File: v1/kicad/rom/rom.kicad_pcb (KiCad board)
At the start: 2 copper layers, 68.5 x 69 mm, 2 parts, among them IC1 AT28C64B-15PU, U1 LNCPU Type A Connector

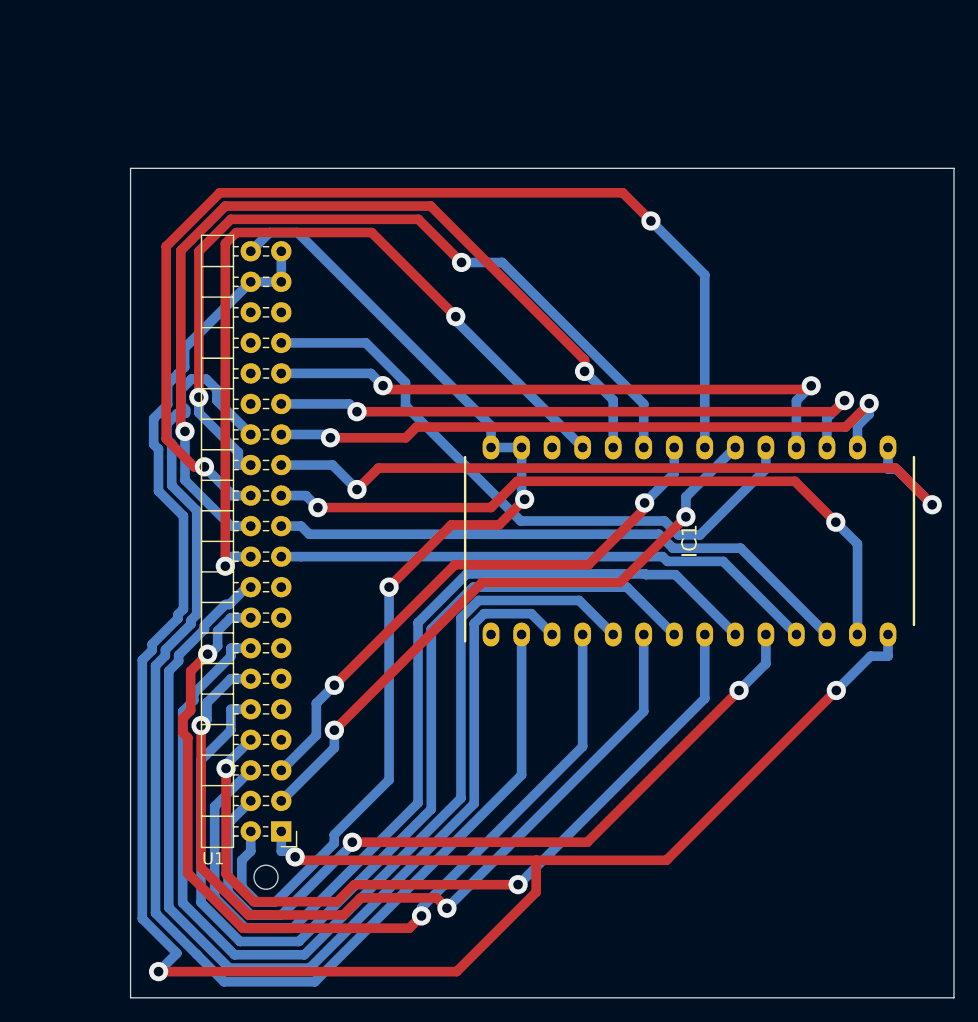
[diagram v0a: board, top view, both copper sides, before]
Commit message: readapt designs for BR, SP, SR, ALU
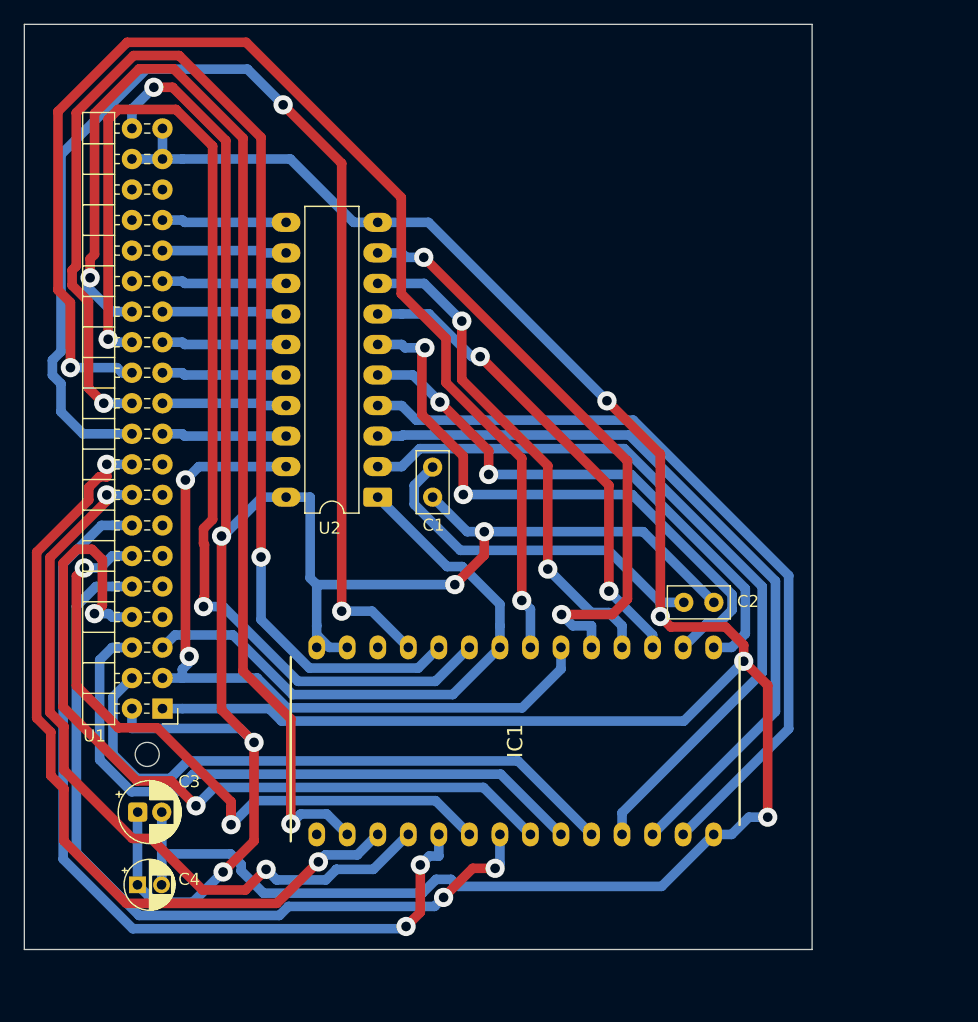
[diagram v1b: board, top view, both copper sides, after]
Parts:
- added C1: 220n, Capacitor_THT:C_Disc_D5.0mm_W2.5mm_P2.50mm, F.Cu at (139.6, 72.4)
- added C2: 220n, Capacitor_THT:C_Disc_D5.0mm_W2.5mm_P2.50mm, F.Cu at (163.0, 81.1)
- added C3: 47u, Capacitor_THT:CP_Radial_D5.0mm_P2.00mm, F.Cu at (115.1, 98.6)
- added C4: 1u, lncpu:CP_Radial_D4.0mm_P2.00mm-Large-Holes, F.Cu at (115.1, 104.6)
- added U2: 74HCT541, Package_DIP:DIP-20_W7.62mm_LongPads, F.Cu at (135.1, 72.4)
- U1: value LNCPU Type A Connector -> LNCPU Type A Header
- moved IC1 22.1 mm to (146.5, 92.6)
- moved U1 14.2 mm to (117.2, 89.9)
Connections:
- U1 pad 19: /DBUS0 -> Net-(U1-DBUS_{0})
- U1 pad 21: /DBUS1 -> Net-(U1-DBUS_{1})
- U1 pad 23: /DBUS2 -> Net-(U1-DBUS_{2})
- U1 pad 25: /DBUS3 -> Net-(U1-DBUS_{3})
- U1 pad 27: /DBUS4 -> Net-(U1-DBUS_{4})
- U1 pad 29: /DBUS5 -> Net-(U1-DBUS_{5})
- U1 pad 31: /DBUS6 -> Net-(U1-DBUS_{6})
- U1 pad 33: /DBUS7 -> Net-(U1-DBUS_{7})
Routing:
- net Net-(IC1-VCC): track 88.7 -> 170.6 mm, vias 2 -> 6
- net Net-(IC1-GND): track 168.1 -> 236.0 mm, vias 3 -> 4
- net Net-(IC1-A8): track 67.2 -> 102.2 mm
- net Net-(IC1-A9): track 75.0 -> 105.2 mm
- net Net-(IC1-A11): track 68.3 -> 95.2 mm
- net Net-(IC1-A1): track 79.3 -> 53.6 mm
- net Net-(IC1-A7): track 85.6 -> 67.8 mm, vias 0 -> 2
- net /DBUS3: track 63.7 -> 46.0 mm
- net /DBUS0: track 45.5 -> 62.8 mm
- net Net-(IC1-A10): track 88.9 -> 105.2 mm
- net Net-(IC1-A3): track 82.1 -> 67.4 mm, vias 0 -> 2
- net /DBUS1: track 49.1 -> 63.5 mm
- net Net-(IC1-A0): track 65.1 -> 50.8 mm, vias 2 -> 0
- net Net-(IC1-A4): track 71.0 -> 57.9 mm
- net Net-(IC1-A6): track 75.6 -> 62.9 mm
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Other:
- board size 68.5 x 69 mm -> 65.5 x 77 mm
